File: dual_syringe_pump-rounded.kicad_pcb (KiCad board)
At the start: 2 copper layers, 100.3 x 85.5 mm, 163 parts, among them J2 Barrel_Jack_Switch_Pin3Ring, Q1 SS8050, Q2 SS8050, Q3 SS8050, Q4 SS8050, U1 ESP32-WROOM-32, U2 AMS1117-3.3, U3 CH340C, U4 TP5100, U5 LM2596S-buck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

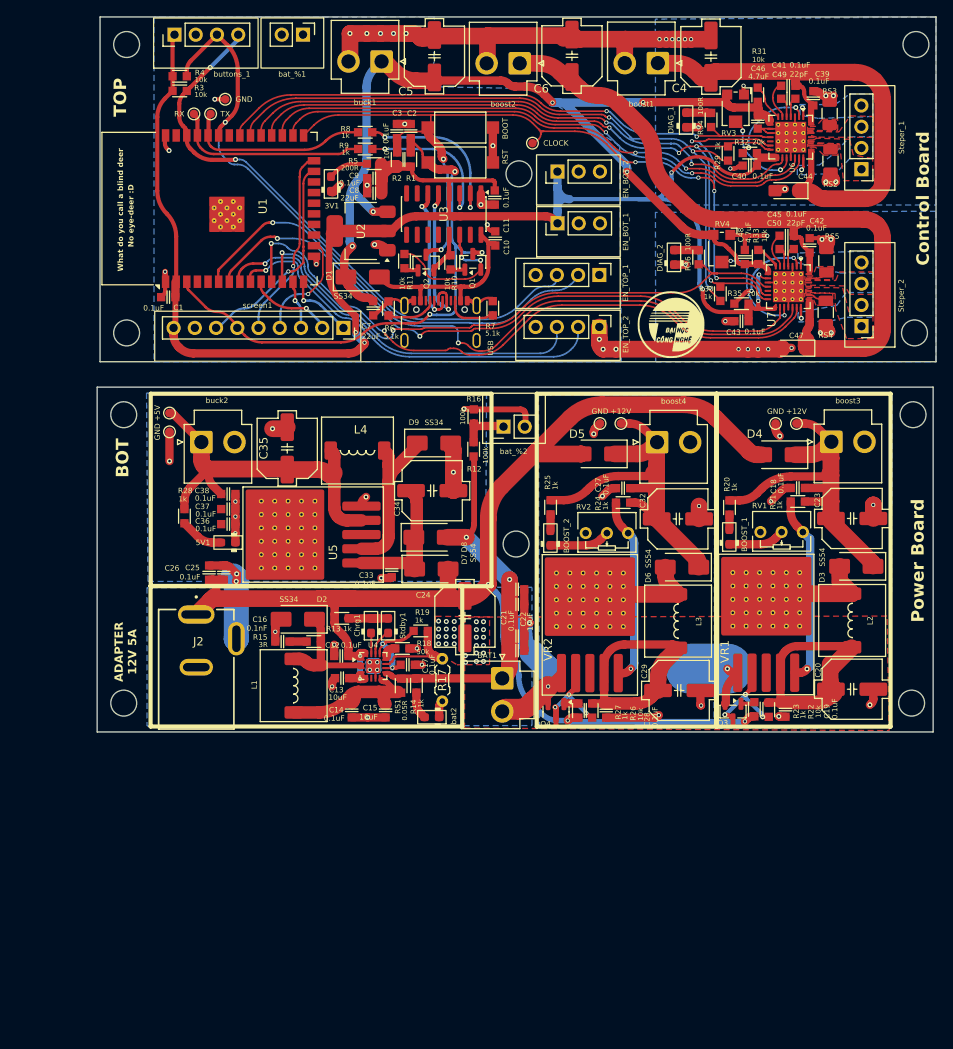
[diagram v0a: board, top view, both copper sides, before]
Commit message: added mousebite to rounded PCB
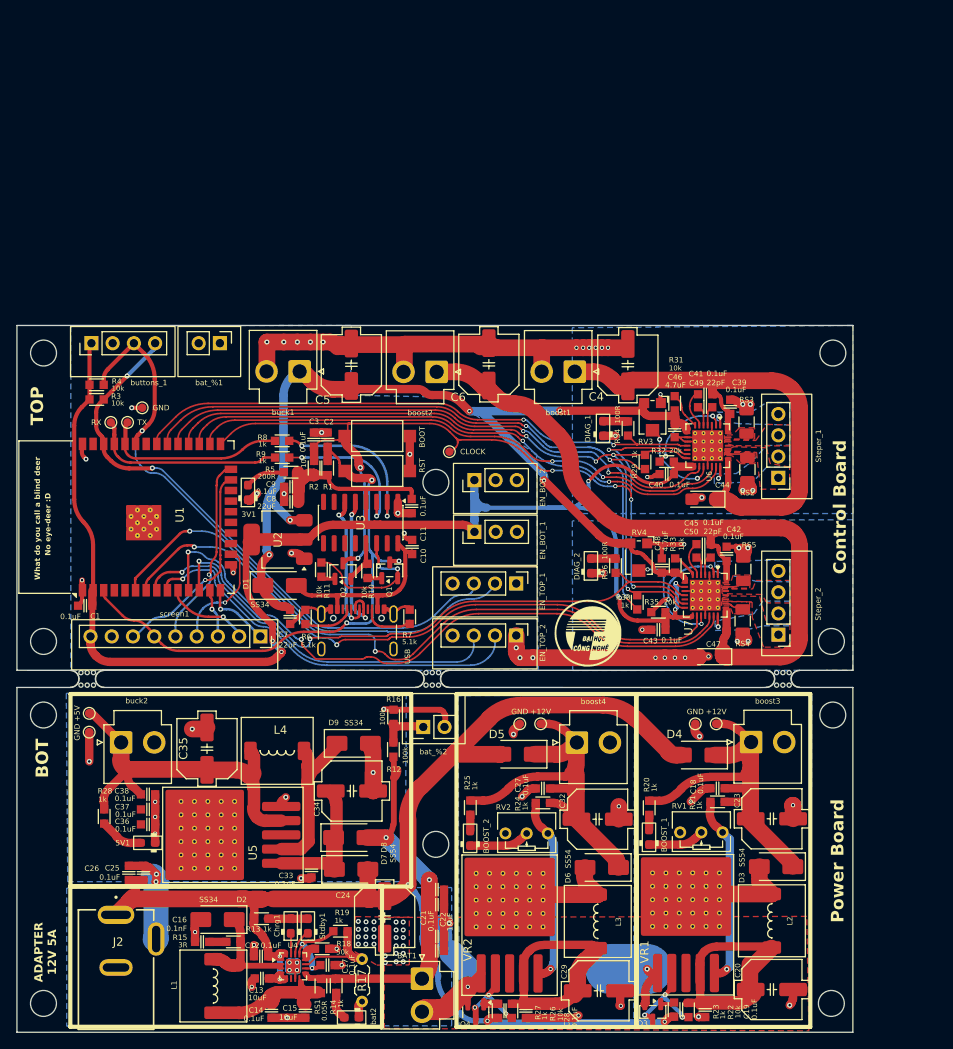
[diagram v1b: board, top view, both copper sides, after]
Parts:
- added mouse-bite-2mm-slot: VAL**, Panelization.pretty-master:mouse-bite-2mm-slot, F.Cu at (141.6, 98.2)
- added mouse-bite-2mm-slot: VAL**, Panelization.pretty-master:mouse-bite-2mm-slot, F.Cu at (58.4, 98.2)
- added mouse-bite-2mm-slot: VAL**, Panelization.pretty-master:mouse-bite-2mm-slot, F.Cu at (99.7, 98.2)
- moved G*** 47.9 mm to (120.0, 120.0)
- moved buck1 38.4 mm to (83.8, 61.4)
- moved C45 38.2 mm to (132.1, 82.1)
- moved RS5 38.2 mm to (136.9, 85.1)
- moved BOOT 38.2 mm to (93.1, 69.2)
- moved C10 38.2 mm to (97.3, 82.4)
- moved C11 38.2 mm to (97.2, 77.6)
- moved C42 38.2 mm to (134.9, 83.3)
- moved C47 38.2 mm to (133.0, 95.6)
- moved C48 38.2 mm to (127.1, 84.7)
- moved C50 38.2 mm to (132.1, 83.7)
- moved D1 38.2 mm to (81.4, 87.1)
- moved DIAG_1 38.2 mm to (120.1, 68.3)
- moved EN_BOT_2 38.2 mm to (104.7, 74.4)
- moved EN_TOP_2 38.2 mm to (109.7, 93.0)
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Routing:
- net Adapter_+12V: track 185.1 -> 178.9 mm
- net +3.3V: track 204.7 -> 206.3 mm
- net +12V_2: track 136.1 -> 135.1 mm
- net Vbat: track 106.4 -> 107.2 mm
- net Net-(Chrg1-A): track 5.55 -> 4.80 mm
- net Net-(D2-K): track 15.6 -> 15.0 mm
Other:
- board size 100.3 x 85.5 mm -> 100 x 84.6 mm

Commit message: Update - 22-Feb-26
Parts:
- R12: value 100k -> 150k
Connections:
- bat_%1 pad 1: unconnected-(bat_%1-Pin_1-Pad1) -> GND1
- bat_%1 pad 2: unconnected-(bat_%1-Pin_2-Pad2) -> /BTN1
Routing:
- net /BTN1: track 0.00 -> 19.9 mm, vias 0 -> 1
- net Adapter_+12V: track 178.9 -> 176.2 mm
- net +3.3V: track 206.3 -> 207.4 mm

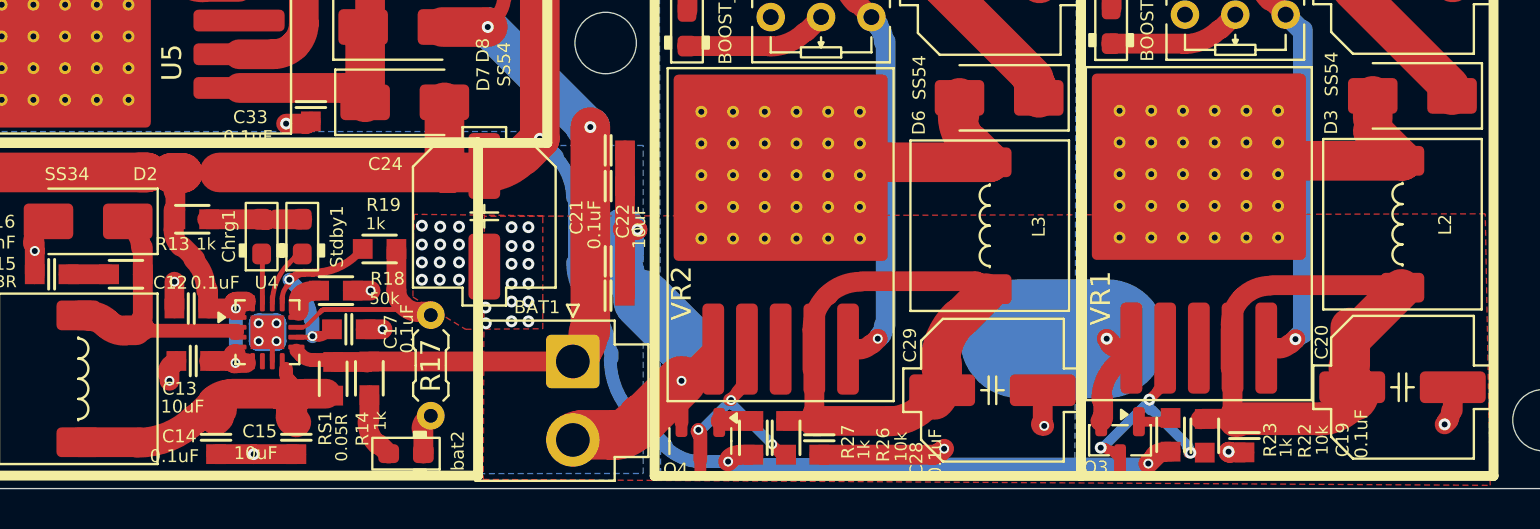
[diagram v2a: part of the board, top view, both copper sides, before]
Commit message: added power button
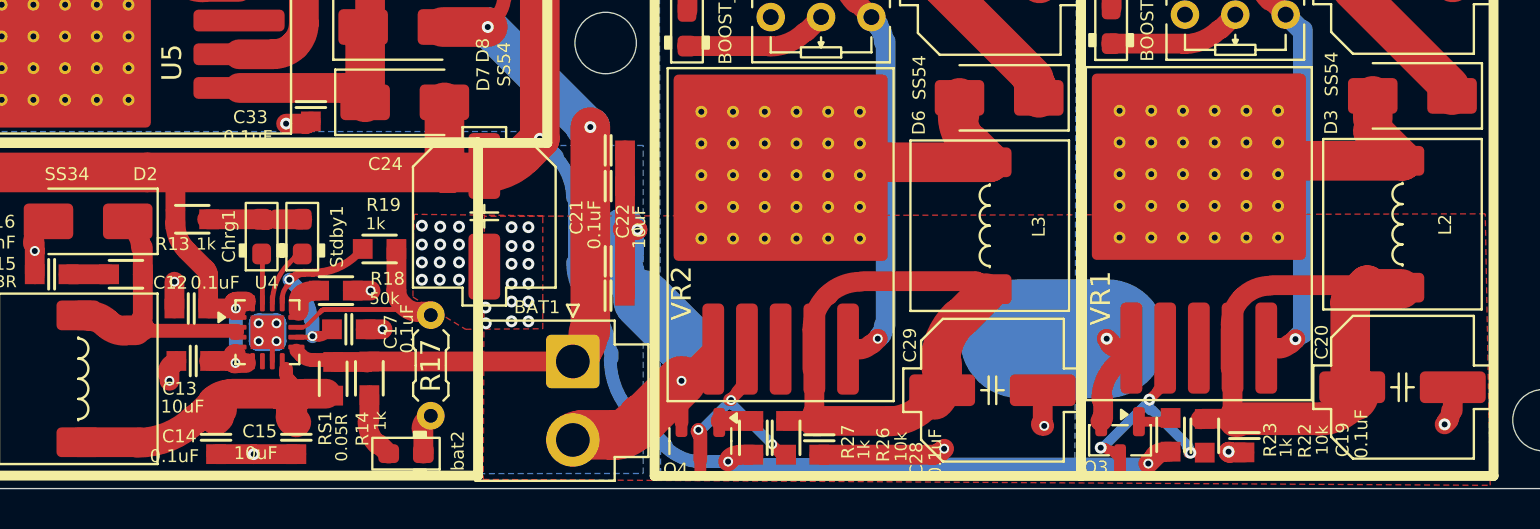
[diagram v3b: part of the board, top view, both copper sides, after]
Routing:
- net Vbat: track 107.0 -> 107.7 mm
